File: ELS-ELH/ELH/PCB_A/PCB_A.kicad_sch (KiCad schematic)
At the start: 44 parts, among them J1 Conn_01x08_Pin, J3 Conn_01x20_Pin, J4 Conn_01x20_Pin, Q1 IRLZ44N, Q2 IRLZ44N, Q4 IRLZ44N, Q6 IRLZ44N

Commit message: Update in symbols and footprints
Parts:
- BOOST1, BOOST2: footprint ELH_Library:TAR-MT3608 -> ELH_Library:XL6009 Boost
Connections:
- net +3.3V: no longer Teensy3.3.3V_1 (3.3V), Teensy3.3.3V_2 (3.3V), Teensy3.3.3V_3 (3.3V)
- net +3.3V_SENSORS: now also Regulator1.OUT (Output); no longer Regulator1.2 (Output)
- net +5VA: no longer Teensy3.VIN
- net +5V_MCU: now also Regulator1.GND; no longer Regulator1.3 (Input)
- net ACTUATOR_POWER_REG_1: now also Regulator3. (OUTPUT+), Regulator4. (OUTPUT+); no longer Regulator3.2 (IN+), Regulator4.4 (OUTPUT+)
- net ACTUATOR_POWER_REG_2: now also Regulator3. (OUTPUT+); no longer Regulator3.4 (OUTPUT+)
- net AIN1: no longer Teensy3.19 (A5)
- net AIN2: no longer Teensy3.17 (A3)
- net BIN1: no longer Teensy3.15 (A1)
- net BIN2: no longer Teensy3.20 (A6)
- net BUZZER2: no longer Teensy3.6 (OUT1D)
- net CH_C_MOSFET_TEENSY_3V3: no longer Teensy3.22 (A8)
- net Ch_D_mosfet_2: no longer Teensy3.36 (CS2)
- net GND: now also Bornera1.2 (Pin_2), Bornera3.2 (Pin_2), Bornera6.1 (Pin_1), Bornera8.1 (Pin_1), Regulator1.IN (Input), Regulator3. (OUTPUT+), Regulator4. (OUTPUT+); no longer Bornera1.1 (Pin_2), Bornera3.1 (Pin_2), Bornera6.2 (Pin_1), Bornera8.2 (Pin_1), Regulator1.1 (GND), Regulator3.1 (IN-), Regulator3.3 (OUTPUT-), Regulator4.1 (IN-), Regulator4.3 (OUTPUT-), Teensy3.GND1 (GND), Teensy3.GND2 (GND), Teensy3.GND3 (GND), Teensy3.GND4 (GND), Teensy3.GND5 (GND)
- net LED4: no longer Teensy3.11 (MOSI)
- net LED5: no longer Teensy3.10 (CS1)
- net LED6: no longer Teensy3.9 (OUT1C)
- net LPWM: no longer Teensy3.13 (SCK)
- net L_EN: no longer Teensy3.40 (A16)
- net L_IS: no longer Teensy3.38 (A14)
- net PWMA: no longer Teensy3.18 (A4)
- net PWMB: no longer Teensy3.14 (A0)
- net RPWM: no longer Teensy3.41 (A17)
- net RX_UART_BUS1_3V3: no longer Teensy3.8 (TX2)
- net R_EN: no longer Teensy3.39 (A15)
- net R_IS: no longer Teensy3.37 (CS3)
- net STBY: no longer Teensy3.16 (A2)
- net TX_UART_BUS1_3V3: no longer Teensy3.7 (RX2)
- net at BOOST1.1 (IN+): now also Bornera6.2 (Pin_2); no longer Bornera6.1 (Pin_2)
- net at BOOST2.3 (OUT+): now also Bornera1.1 (Pin_1); no longer Bornera1.2 (Pin_1)
- net at BOOST2.1 (IN+): now also Bornera8.2 (Pin_2); no longer Bornera8.1 (Pin_2)
- removed net USB_GND: Teensy3.USB_GND1 (USB_GND), Teensy3.USB_GND2 (USB_GND)
- new net: Bornera3.1 (Pin_1), Regulator4. (OUTPUT+)
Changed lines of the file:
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@@
 	)
 	(symbol
-		(lib_name "Screw_Terminal_01x02_2")
 		(lib_id "Connector:Screw_Terminal_01x02")
 		(at 153.67 -39.37 180)
@@
 			)
 		)
-		(pin "1"
+		(pin ""
 		)
-		(pin "3"
+		(pin ""
 		)
-		(pin "2"
+		(pin ""
 		)
-		(pin "4"
+		(pin ""
 		)
 		(instances
@@
 	)
 	(symbol
-		(lib_name "Screw_Terminal_01x02_1")
 		(lib_id "Connector:Screw_Terminal_01x02")
 		(at 64.77 161.29 0)
@@
 	)
 	(symbol
-		(lib_name "Screw_Terminal_01x02_1")
 		(lib_id "Connector:Screw_Terminal_01x02")
 		(at 111.76 -44.45 0)
@@
 	)
 	(symbol
+		(lib_name "MP1584_1")
 		(lib_id "ELH_Library:MP1584")
 		(at 177.8 -85.09 0)
@@
 			)
 		)
-		(pin "1"
+		(pin ""
 		)
-		(pin "3"
+		(pin ""
 		)
-		(pin "2"
+		(pin ""
 		)
-		(pin "4"
+		(pin ""
 		)
 		(instances
@@
 	)
 	(symbol
-		(lib_name "Screw_Terminal_01x02_4")
 		(lib_id "Connector:Screw_Terminal_01x02")
 		(at 64.77 153.67 0)
@@
 	)
 	(symbol
-		(lib_name "Screw_Terminal_01x02_2")
 		(lib_id "Connector:Screw_Terminal_01x02")
 		(at 210.82 29.21 0)
@@
 	)
 	(symbol
-		(lib_name "Teensy 4.1_2")
 		(lib_id "ELH_Library:Teensy 4.1")
-		(at 396.24 -34.29 180)
+		(at 398.78 62.23 180)
 		(unit 1)
 		(body_style 1)
@@
 		(fields_autoplaced yes)
 		(property "Reference" "Teensy3"
-			(at 411.48 17.78 0)
+			(at 414.02 114.3 0)
 			(hide yes)
 			(show_name no)
@@
 		)
 		(property "Value" "Teensy 4.1"
-			(at 396.24 19.05 0)
+			(at 398.78 115.57 0)
 			(show_name no)
 			(do_not_autoplace no)
@@
 		)
 		(property "Footprint" "ELH_Library:Teensy 4.1"
-			(at 396.24 -34.29 0)
+			(at 398.78 62.23 0)
 			(hide yes)
 			(show_name no)
@@
 		)
 		(property "Datasheet" "https://www.alldatasheet.es/datasheet-pdf/view/1358265/SPARKFUN/DEV-16771.html"
-			(at 396.24 -34.29 0)
+			(at 398.78 62.23 0)
 			(hide yes)
 			(show_name no)
@@
 		)
 		(property "Description" "Microcontroller"
-			(at 396.24 -34.29 0)
+			(at 398.78 62.23 0)
 			(hide yes)
 			(show_name no)
@@
 		)
 		(property "Price" ""
-			(at 396.24 -34.29 0)
+			(at 398.78 62.23 0)
 			(hide yes)
 			(show_name no)
@@
 		(pin "21"
 		)
-		(pin "ON/OFF"
+		(pin "GND"
 		)
 		(pin "7"
@@
 		(pin "15"
 		)
-		(pin "PROGRAM"
+		(pin "3V3"
 		)
 		(pin "17"
@@
 		(pin "40"
 		)
-		(pin "D-"
-		)
 		(pin "27"
 		)
-		(pin "T+"
-		)
 		(pin "32"
 		)
 		(pin "9"
 		)
-		(pin "3.3V_3"
-		)
-		(pin "3.3V_2"
-		)
-		(pin "3.3V_1"
-		)
 		(pin "22"
 		)
-		(pin "5V"
-		)
-		(pin "VUSB"
-		)
-		(pin "LED"
-		)
-		(pin "T-"
-		)
-		(pin "VBAT"
-		)
-		(pin "R-"
-		)
-		(pin "R+"
-		)
-		(pin "D+"
-		)
 		(pin "2"
 		)
@@
 		(pin "24"
 		)
-		(pin "GND1"
-		)
-		(pin "GND2"
-		)
 		(pin "23"
 		)
-		(pin "GND3"
-		)
-		(pin "GND4"
-		)
-		(pin "GND5"
-		)
-		(pin "USB_GND1"
-		)
-		(pin "USB_GND2"
-		)
 		(instances
 			(project "PCB_A"
@@
 			)
 		)
-		(pin "2"
+		(pin "GND"
 		)
-		(pin "3"
+		(pin "IN"
 		)
-		(pin "1"
+		(pin "OUT"
 		)
 		(instances
@@
 	)
 	(symbol
-		(lib_name "Screw_Terminal_01x02_1")
 		(lib_id "Connector:Screw_Terminal_01x02")
 		(at 110.49 -82.55 0)
@@
 			)
 		)
-		(property "Footprint" "ELH_Library:TAR-MT3608"
+		(property "Footprint" "ELH_Library:XL6009 Boost"
 			(at 176.53 -44.45 0)
 			(hide yes)
@@
 			)
 		)
-		(property "Footprint" "ELH_Library:TAR-MT3608"
+		(property "Footprint" "ELH_Library:XL6009 Boost"
 			(at 187.96 26.67 0)
 			(hide yes)
@@
 	)
 	(symbol
-		(lib_name "Screw_Terminal_01x02_2")
 		(lib_id "Connector:Screw_Terminal_01x02")
 		(at 171.45 31.75 180)

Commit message: Update on schematics B
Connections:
- net +5VA is gone; now on net +5V_MCU: C1.2, C3.1
- net LPWM is gone; now on net LPWM_BTS7960_3V3: J1.8 (Pin_8)
- net L_EN is gone; now on net L_EN_BTS7960_3V3: J1.6 (Pin_6)
- net L_IS is gone; now on net L_IS_BTS7960_3V3: J1.4 (Pin_4)
- net RPWM is gone; now on net RPWM_BTS7960_3V3: J1.7 (Pin_7)
- net R_EN is gone; now on net R_EN_BTS7960_3V3: J1.5 (Pin_5)
- net R_IS is gone; now on net R_IS_BTS7960_3V3: J1.3 (Pin_3)
- net +5V_MCU: now also Teensy3.VIN (Vin)
- net BUZZER_SIGNAL_3V3: now also Teensy3.5 (5/IN2/PWM)
- net CH_C_MOSFET_TEENSY_3V3: now also Teensy3.14 (14/A0/TX3/S/PDIF_OUT/PWM)
- net CH_D_MOSFET_TEENSY_3V3: now also Teensy3.15 (15/A1/RX3/S/PDIF_IN/PWM)
- net GND: now also Teensy3.GND
- net LED_BLUE_SIGNAL_3V3: now also Teensy3.2 (2/OUT2/PWM)
- net LED_GREEN_SIGNAL_3V3: now also Teensy3.3 (3/LRCLK2/PWM)
- net LED_RED_SIGNAL_3V3: now also Teensy3.4 (4/BCLK2/PWM)
- net RX_UART_BUS1_3V3: now also Teensy3.8 (8/TX2/IN1/PWM)
- net TX_UART_BUS1_3V3: now also Teensy3.7 (7/RX2/OUT1A/PWM)
- net LPWM_BTS7960_3V3: now reaches Teensy3.28 (28/RX7/PWM)
- net RPWM_BTS7960_3V3: now reaches Teensy3.29 (29/TX7/PWM)
- net L_EN_BTS7960_3V3: now reaches Teensy3.31 (31/CTX3)
- net R_EN_BTS7960_3V3: now reaches Teensy3.32 (32/OUT1B)
- net R_IS_BTS7960_3V3: now reaches Teensy3.34 (34/RX8)
- net L_IS_BTS7960_3V3: now reaches Teensy3.35 (35/TX8)
- no-connect marks 34 -> 0

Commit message: Update in schematic A
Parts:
- removed Bornera2: Ch.A Output, ELH_Library:Bornera 2P, symbol Connector:Screw_Terminal_01x02
- removed Bornera7: Ch.B Output, ELH_Library:Bornera 2P, symbol Connector:Screw_Terminal_01x02
- removed C4: 10uF, Capacitor_THT:CP_Radial_D5.0mm_P2.00mm, symbol Device:C_Polarized_Small
- removed Driver_DC2: TB6612FNG, ELH_Library:TB6612FNG, symbol ELH_Library:TB6612FNG
- removed Teensy3: Teensy 4.1, ELH_Library:Teensy 4.1, symbol ELH_Library:Teensy 4.1
- added Bornera10: Ch. B Output, ELH_Library:Bornera 2P, symbol Connector:Screw_Terminal_01x02
- added Bornera11: Ch.A Output, ELH_Library:Bornera 2P, symbol Connector:Screw_Terminal_01x02
- added Bornera9: PWR 4, ELH_Library:Bornera 2P, symbol Connector:Screw_Terminal_01x02
- added C11, C12: 47uF, Capacitor_THT:CP_Radial_D6.3mm_P2.50mm, symbol Device:C_Polarized_Small
- added C5, C6: 100nF, Capacitor_THT:C_Disc_D5.0mm_W2.5mm_P5.00mm, symbol Device:C_Small
- added C7: 10uF, Capacitor_THT:CP_Radial_D5.0mm_P2.00mm, symbol Device:C_Polarized_Small
- added D2, D4: 1N4007, Diode_THT:D_DO-41_SOD81_P10.16mm_Horizontal, symbol Diode:1N4007
- added ESP1: ESP32 DEVKIT V1, ELH_Library:ESP32 DEVKIT V1, symbol ELH_Library:ESP32 DEVKIT V1
- added Q3, Q5: IRLZ44N, Package_TO_SOT_THT:TO-220-3_Vertical, symbol Transistor_FET:IRLZ44N
- added R12, R13: (no value), Resistor_THT:R_Axial_DIN0207_L6.3mm_D2.5mm_P7.62mm_Horizontal, symbol Device:R_US
- added R21, R23: 220, Resistor_THT:R_Axial_DIN0207_L6.3mm_D2.5mm_P7.62mm_Horizontal, symbol Device:R_US
- added R22, R24: 10K, Resistor_THT:R_Axial_DIN0207_L6.3mm_D2.5mm_P7.62mm_Horizontal, symbol Device:R_US
- Bornera1: value Camera Connection -> PWR 2 REG
- Bornera3: value Actuator Power Supply -> PWR 3
- Bornera6: value Sensor Power Supply -> PWR 1
- Bornera8: value Camera Power Supply -> PWR 2
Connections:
- net ACTUATOR_POWER_REG_2 is gone; now on net PWR 4 REG: Regulator3. (OUTPUT+)
- net +3.3V_SENSORS: now also C7.1
- net +5V_MCU: now also Regulator1.IN (Input), ESP1.VIN; no longer Regulator1.GND
- net GND: now also Regulator1.GND, Bornera9.2 (Pin_2), C7.2, ESP1.GND, Q3.3 (S), Q5.3 (S), R22.2, R24.2; no longer Regulator1.IN (Input)
- net LED_BLUE_SIGNAL_3V3: now also ESP1.D32
- net LED_GREEN_SIGNAL_3V3: now also ESP1.D33
- net LED_RED_SIGNAL_3V3: now also ESP1.D13
- net LPWM_BTS7960_3V3: now also ESP1.D26
- net L_EN_BTS7960_3V3: now also ESP1.D14
- net L_IS_BTS7960_3V3: now also C6.1, ESP1.D35, R13.1
- net RPWM_BTS7960_3V3: now also ESP1.D25
- net RX_UART_BUS1_3V3: now also ESP1.D23
- net R_EN_BTS7960_3V3: now also ESP1.D27
- net R_IS_BTS7960_3V3: now also C5.2, ESP1.D34, R12.1
- net TX_UART_BUS1_3V3: now also ESP1.D5
- net +5V: no longer names the net of J4.1 (Pin_1), J4.2 (Pin_2), J4.3 (Pin_3)
- net +5V: no longer J3.5 (Pin_5), J3.6 (Pin_6), J3.7 (Pin_7)
- net ACTUATOR_POWER_REG_1 renamed PWR 4 REG
- net PWR 4 REG: no longer Regulator4. (OUTPUT+)
- net CH_C_MOSFET_TEENSY_3V3 renamed CH_C_MOSFET_ESP2_3V3
- net CH_C_MOSFET_ESP2_3V3: now also ESP1.D19
- net CH_D_MOSFET_TEENSY_3V3 renamed CH_D_MOSFET_ESP2_3V3
- net CH_D_MOSFET_ESP2_3V3: now also ESP1.D18
- new net: Q5.1 (G), R23.2, R24.1
- new net: Bornera11.1 (Pin_1), C12.2, D4.2 (A), Q5.2 (D)
- new net: Bornera9.1 (Pin_1), Regulator3. (OUTPUT+)
- new net: C5.1, R12.2
- new net: C6.2, R13.2
- new net: Q3.1 (G), R21.2, R22.1
- new net: Bornera10.1 (Pin_1), C11.2, D2.2 (A), Q3.2 (D)
- new net: J3.5 (Pin_5), J3.6 (Pin_6), J3.7 (Pin_7)
- new net CH_A_MOSFET_ESP2_3V3: ESP1.TX2 (D17/TX2), R23.1
- new net CH_B_MOSFET_ESP2_3V3: ESP1.RX2 (D16/RX2), R21.1
- new net PWR 3 REG: Bornera10.2 (Pin_2), Bornera11.2 (Pin_2), C11.1, C12.1, D2.1 (K), D4.1 (K), Regulator4. (OUTPUT+)
- new net SCL_I2C_BUS1_3V3: ESP1.D22
- new net SDA_I2C_BUS1_3V3: ESP1.D21
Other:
- note removed: "BUZZER CTR OBC"
- note removed: "CTR OBC (Teensy 4.1)"
- note removed: "Circuit for the MOSFETs of Solenoid Valve 1"
- note removed: "Circuit for the MOSFETs of Solenoid Valve 2"
- note removed: "Headers"
- note removed: "LEDs CTR OBC"
- note removed: "Power Supply"
- note removed: "Reaction Wheels"
- note removed: "Regulator 5V - 3.3V"
- note removed: "Voltage Boost Circuit for Camera"
- note removed: "Voltage Boost Circuit for Sensors"
- note removed: "Voltage Regulator Circuit for Actuators"
- note removed: "Voltage Regulator Circuit for LM1117T"
- moved on the sheet: J1, J3, J4, Q1, Q4, R10, R11, R16, R18, R19, R20, R3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

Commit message: PCB B Almost finishhed
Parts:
- removed BOOST1, BOOST2: TAR-MT3608, ELH_Library:XL6009 Boost, symbol ELH_Library:XL6009_Boost
- removed BZ2: Buzzer, Buzzer_Beeper:Buzzer_12x9.5RM7.6, symbol Device:Buzzer
- removed C1, C5, C6: 100nF, Capacitor_THT:C_Disc_D5.0mm_W2.5mm_P5.00mm, symbol Device:C_Small
- removed C3: 10uF, Capacitor_THT:CP_Radial_D5.0mm_P2.50mm, symbol Device:C_Polarized_Small
- removed D3: LED_RKGB, LED_THT:LED_D5.0mm-4_RGB_Staggered_Pins, symbol Device:LED_RKGB
- removed ESP1: ESP32 DEVKIT V1, ELH_Library:ESP32 DEVKIT V1, symbol ELH_Library:ESP32 DEVKIT V1
- removed J1: Conn_01x08_Pin, Connector_PinSocket_2.54mm:PinSocket_1x08_P2.54mm_Vertical, symbol Connector:Conn_01x08_Pin
- removed R1, R2, R8: 330, Resistor_THT:R_Axial_DIN0207_L6.3mm_D2.5mm_P7.62mm_Horizontal, symbol Device:R_US
- removed R12, R13: (no value), Resistor_THT:R_Axial_DIN0207_L6.3mm_D2.5mm_P7.62mm_Horizontal, symbol Device:R_US
- removed R9: 220, Resistor_THT:R_Axial_DIN0207_L6.3mm_D2.5mm_P7.62mm_Horizontal, symbol Device:R_US
- added BOOST1, BOOST2: TAR-MT3608, ELH_Library:TAR-MT3608, symbol ELH_Library:TAR-MT3608
- C10: renamed from C11; value 47uF -> C_Polarized_Small
- C4: renamed from C2; value 10uF -> C_Polarized_Small
- C6: renamed from C7; value 10uF -> C_Polarized_Small
- C7: renamed from C9; value 47uF -> C_Polarized_Small
- C8: renamed from C10; value 47uF -> C_Polarized_Small
- C9: renamed from C12; value 47uF -> C_Polarized_Small
- J1: renamed from Bornera6; value PWR 1 -> Screw_Terminal_01x02
- J10: renamed from Bornera4; value Ch.C Output -> Screw_Terminal_01x02
- J11: renamed from Bornera11; value Ch.A Output -> Screw_Terminal_01x02
- J12: renamed from Bornera10; value Ch. B Output -> Screw_Terminal_01x02
- J2: renamed from Bornera8; value PWR 2 -> Screw_Terminal_01x02
- J3: renamed from Bornera3; value PWR 3 -> Screw_Terminal_01x02
- J4: renamed from Bornera9; value PWR 4 -> Screw_Terminal_01x02
- J5: renamed from Bornera1; value PWR 2 REG -> Screw_Terminal_01x02
- J9: renamed from Bornera5; value Ch.D Output -> Screw_Terminal_01x02
- R10: renamed from R3; value 220 -> R_US
- R11: renamed from R16; value 220 -> R_US
- R12: renamed from R6; value 220 -> R_US
- R13: renamed from R22; value 10K -> R_US
- R14: renamed from R24; value 10K -> R_US
- R15: renamed from R18; value 10K -> R_US
- R16: renamed from R19; value 10K -> R_US
- R17: renamed from R10; value 10K -> R_US
- R18: renamed from R11; value 10K -> R_US
- R7: renamed from R21; value 220 -> R_US
- R8: renamed from R23; value 220 -> R_US
- R9: renamed from R20; value 220 -> R_US
- Regulator1: renamed from Regulator4; value LM2596 -> MP1584
- Regulator2: renamed from Regulator3; value LM2596 -> MP1584
- renumbered D9 to D2, D1 to D3, D2 to D5, J3 to J6, J4 to J8, Q3 to Q1, Q5 to Q2, Q6 to Q3, Q2 to Q4, Q1 to Q5, Q4 to Q6, Regulator1 to Regulator3
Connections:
- net +5V_MCU: now also BOOST1.3 (OUT+)
- net GND: now also Regulator1.IN-, Regulator1.OUT- (OUTPUT-), Regulator2.IN-, Regulator2.OUT- (OUTPUT-), BOOST1.2 (IN-), BOOST1.4 (OUT-), BOOST2.2 (IN-), BOOST2.4 (OUT-); no longer Regulator1. (OUTPUT+), Regulator2. (OUTPUT+)
- net PWR 3 REG: now also Regulator1.OUT+ (OUTPUT+); no longer Regulator1. (OUTPUT+)
- net PWR 4 REG: now also Regulator2.OUT+ (OUTPUT+); no longer Regulator2. (OUTPUT+)
- net at J1.2 (Pin_2): now also BOOST1.1 (IN+)
- net at J3.1 (Pin_1): now also Regulator1.IN+; no longer Regulator1. (OUTPUT+)
- net at J4.1 (Pin_1): now also Regulator2.IN+; no longer Regulator2. (OUTPUT+)
- net at J2.2 (Pin_2): now also BOOST2.1 (IN+)
- net at J5.1 (Pin_1): now also BOOST2.3 (OUT+)

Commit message: PCB B ready, PCB A layout ready
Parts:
- removed J8: Conn_01x20_Pin, Connector_PinHeader_2.54mm:PinHeader_1x20_P2.54mm_Vertical, symbol Connector:Conn_01x20_Pin
- added J7: Conn_01x20_Pin, Connector_PinHeader_2.54mm:PinHeader_1x20_P2.54mm_Vertical, symbol Connector:Conn_01x20_Pin
- J1: value Screw_Terminal_01x02 -> PWR 1
- J10: value Screw_Terminal_01x02 -> CH C OUT
- J11: value Screw_Terminal_01x02 -> CH A OUT
- J12: value Screw_Terminal_01x02 -> CH B OUT
- J2: value Screw_Terminal_01x02 -> PWR 2
- J3: value Screw_Terminal_01x02 -> PWR 3
- J4: value Screw_Terminal_01x02 -> PWR 4
- J5: value Screw_Terminal_01x02 -> PWR 2 OUT
- J9: value Screw_Terminal_01x02 -> CH D OUT
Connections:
- net RX_UART_BUS1_3V3 is gone; now on net CH_C_MOSFET_ESP_MAIN_3V3: J6.13 (Pin_13), J6.14 (Pin_14), J6.15 (Pin_15)
- net TX_UART_BUS1_3V3 is gone; now on net +3.3V_SENSORS: J6.17 (Pin_17), J6.18 (Pin_18), J6.19 (Pin_19)
- net +3.3V_SENSORS: now also J6.20 (Pin_20), J7.1 (Pin_1), J7.19 (Pin_19), J7.20 (Pin_20); no longer J6.10 (Pin_10), J6.11 (Pin_11), J6.9 (Pin_9)
- net +5V_MCU: now also J6.4 (Pin_4); no longer J6.1 (Pin_1)
- net GND: now also J6.1 (Pin_1), J6.5 (Pin_5), J6.6 (Pin_6), J6.7 (Pin_7), J7.10 (Pin_10), J7.14 (Pin_14), J7.18 (Pin_18), J7.2 (Pin_2), J7.6 (Pin_6); no longer J6.20 (Pin_20), J6.4 (Pin_4)
- net CH_A_MOSFET_ESP2_3V3 renamed CH_A_MOSFET_ESP_CTR_3V3
- net CH_A_MOSFET_ESP_CTR_3V3: now also J7.7 (Pin_7), J7.8 (Pin_8), J7.9 (Pin_9)
- net CH_C_MOSFET_ESP2_3V3 renamed CH_C_MOSFET_ESP_CTR_3V3
- net CH_C_MOSFET_ESP_CTR_3V3: now also J7.15 (Pin_15), J7.16 (Pin_16), J7.17 (Pin_17)
- net CH_C_MOSFET_ESP_3V3 renamed CH_C_MOSFET_ESP_MAIN_3V3
- net CH_D_MOSFET_ESP2_3V3 renamed CH_D_MOSFET_ESP_CTR_3V3
- net CH_D_MOSFET_ESP_CTR_3V3: now also J7.11 (Pin_11), J7.12 (Pin_12), J7.13 (Pin_13)
- net CH_D_MOSFET_ESP_3V3 renamed CH_D_MOSFET_ESP_MAIN_3V3
- net CH_D_MOSFET_ESP_MAIN_3V3: now also J6.10 (Pin_10), J6.11 (Pin_11), J6.9 (Pin_9)
- new net CH_B_MOSFET_ESP_CTR_3V3: J7.3 (Pin_3), J7.4 (Pin_4), J7.5 (Pin_5)

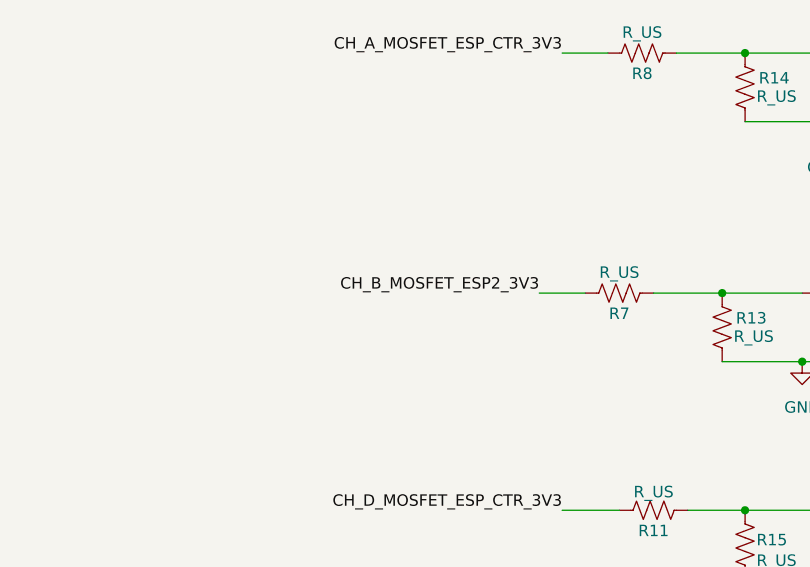
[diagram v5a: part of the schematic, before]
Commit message: PCB A routed
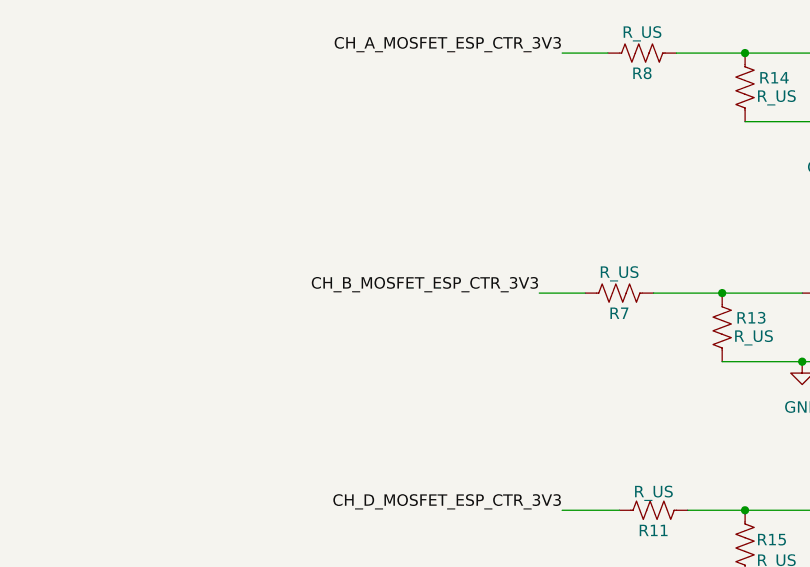
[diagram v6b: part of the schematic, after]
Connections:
- net CH_B_MOSFET_ESP2_3V3 is gone; now on net CH_B_MOSFET_ESP_CTR_3V3: R7.1

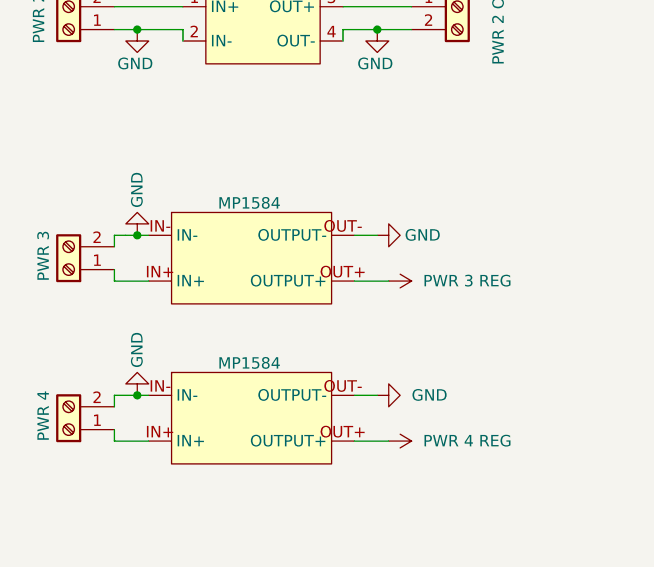
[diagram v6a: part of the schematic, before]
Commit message: regulator's names changed
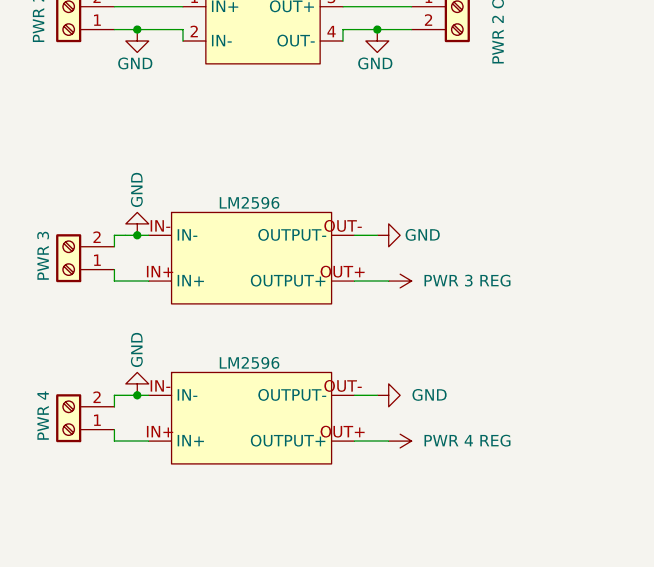
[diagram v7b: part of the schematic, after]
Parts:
- Regulator1, Regulator2: value MP1584 -> LM2596
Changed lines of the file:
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@@
 			)
 		)
-		(property "Value" "MP1584"
+		(property "Value" "LM2596"
 			(at 49.276 70.104 0)
 			(show_name no)
@@
 			)
 		)
-		(property "Value" "MP1584"
+		(property "Value" "LM2596"
 			(at 49.276 87.884 0)
 			(show_name no)

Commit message: Update almost finished
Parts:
- C10, C7, C8, C9: value C_Polarized_Small -> 47uF
- C4, C6: value C_Polarized_Small -> 10uF
- J1: value PWR 1 -> PWR 1 IN
- J2: value PWR 2 -> PWR 2 IN
- J3: value PWR 3 -> PWR 3 IN
- J4: value PWR 4 -> PWR 4 IN
- R10, R11, R12, R7, R8: value R_US -> 220
- R13, R14, R15, R16, R17, R18: value R_US -> 10K
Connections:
- net CH_A_MOSFET_ESP_CTR_3V3: now also J7.15 (Pin_15), J7.16 (Pin_16), J7.17 (Pin_17); no longer J7.7 (Pin_7), J7.8 (Pin_8), J7.9 (Pin_9)
- net CH_C_MOSFET_ESP_CTR_3V3: now also J7.7 (Pin_7), J7.8 (Pin_8), J7.9 (Pin_9); no longer J7.15 (Pin_15), J7.16 (Pin_16), J7.17 (Pin_17)
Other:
- moved on the sheet: C4, C6
